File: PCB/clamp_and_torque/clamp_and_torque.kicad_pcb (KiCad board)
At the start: 2 copper layers, 4 parts, among them J3 LimitSwitches

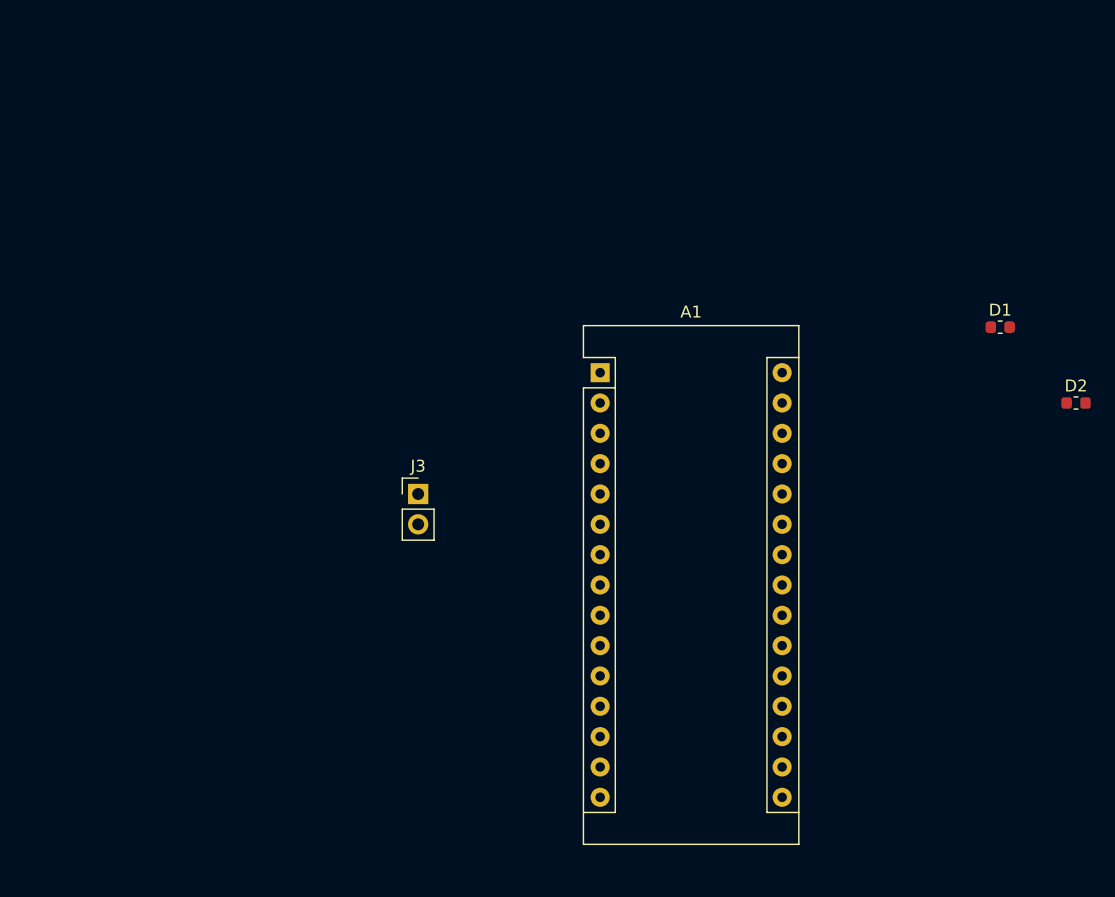
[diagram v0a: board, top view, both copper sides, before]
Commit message: Update some footprints and add a few more components.
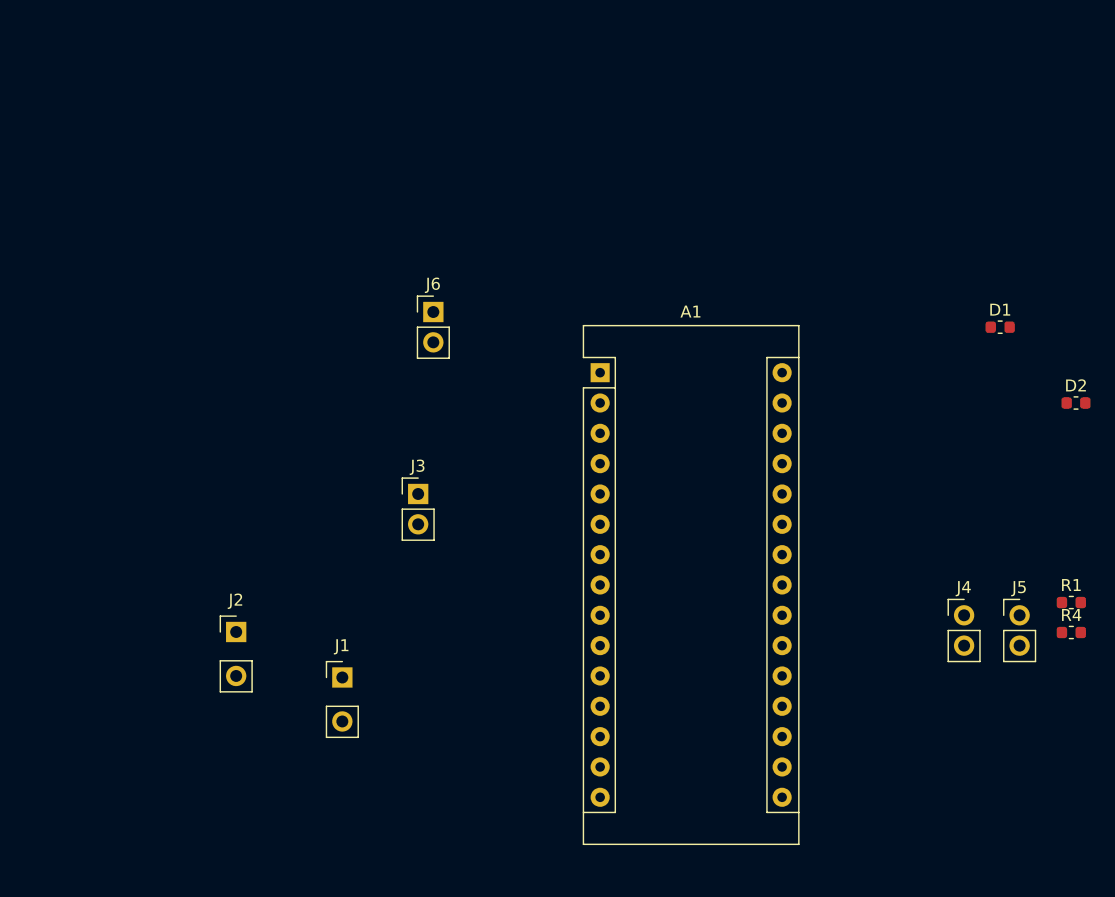
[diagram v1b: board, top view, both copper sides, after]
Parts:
- added J1: Servo1, Connector_PinHeader_2.54mm:PinHeader_1x02_P5.04mm_Vertical, F.Cu at (123.2, 125.7)
- added J2: Servo2, Connector_PinHeader_2.54mm:PinHeader_1x02_P5.04mm_Vertical, F.Cu at (114.3, 121.9)
- added J4: Conn_01x02_Female, Connector_PinHeader_2.54mm:PinHeader_1x02_P2.54mm_Vertical_V2, F.Cu at (175.3, 119.4)
- added J5: Conn_01x02_Female, Connector_PinHeader_2.54mm:PinHeader_1x02_P2.54mm_Vertical_V2, F.Cu at (179.9, 119.4)
- added J6: LimitSwitchB, Connector_PinHeader_2.54mm:PinHeader_1x02_P2.54mm_Vertical, F.Cu at (130.8, 94.0)
- added R1: 10k, Resistor_SMD:R_0603_1608Metric, F.Cu at (184.2, 118.3)
- added R4: 10k, Resistor_SMD:R_0603_1608Metric, F.Cu at (184.2, 120.8)
- J3: value LimitSwitches -> LimitSwitchA
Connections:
- A1 pad 29: Net-(A1-Pad29) -> GND
- A1 pad 5: Net-(A1-Pad5) -> D2
- A1 pad 6: Net-(A1-Pad6) -> D3
- J3 pad 1: Net-(A1-Pad6) -> GND
- J3 pad 2: Net-(A1-Pad5) -> D3

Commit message: Cleaned up schematic and roughly placed all components.
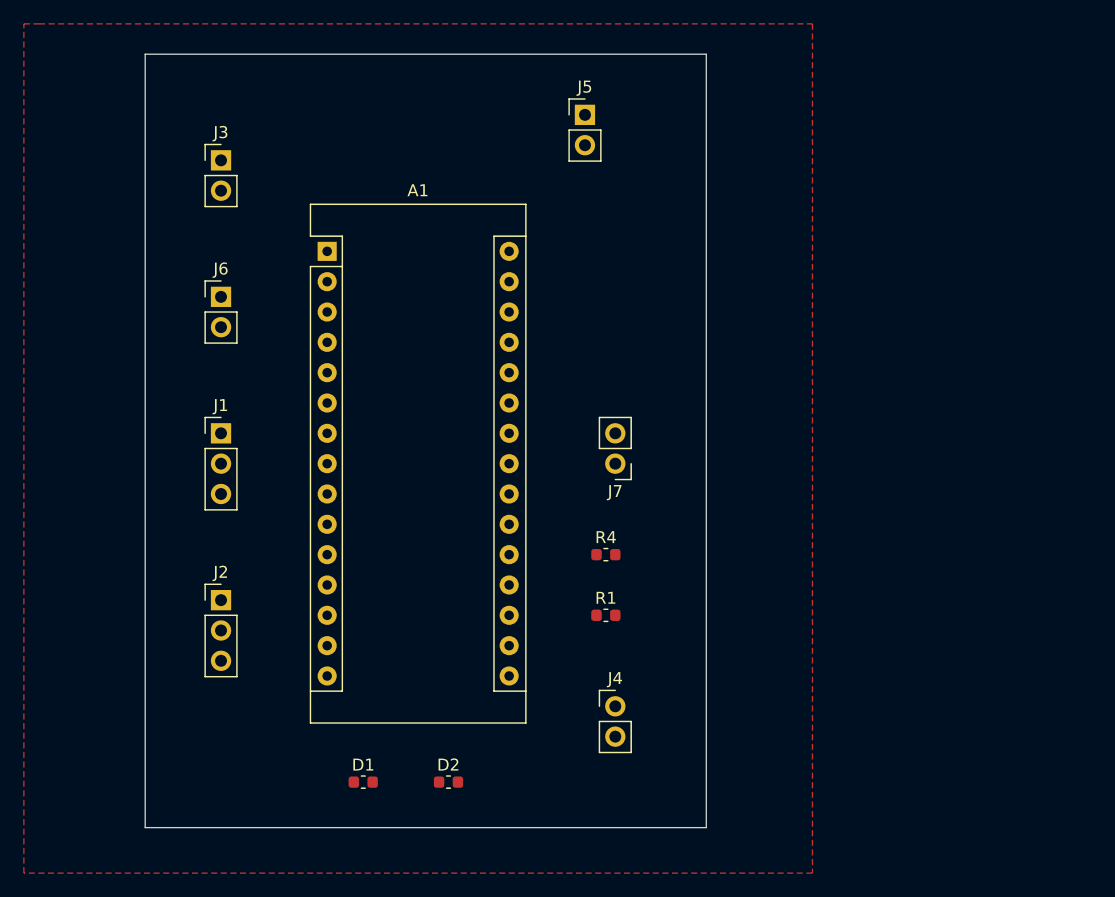
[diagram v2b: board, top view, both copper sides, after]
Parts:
- added J7: Conn_01x02_Female, Connector_PinHeader_2.54mm:PinHeader_1x02_P2.54mm_Vertical_V2, F.Cu at (146.1, 106.7)
- J1, J2: footprint Connector_PinHeader_2.54mm:PinHeader_1x02_P5.04mm_Vertical -> Connector_PinHeader_2.54mm:PinHeader_1x03_P2.54mm_Vertical
- J5: footprint Connector_PinHeader_2.54mm:PinHeader_1x02_P2.54mm_Vertical_V2 -> Connector_PinHeader_2.54mm:PinHeader_1x02_P2.54mm_Vertical
- moved D1 65.5 mm to (124.9, 133.3)
- moved D2 61.4 mm to (132.1, 133.3)
- moved J5 55.5 mm to (143.5, 77.5)
- moved R4 39.5 mm to (145.3, 114.3)
- moved R1 39.0 mm to (145.3, 119.4)
- moved J3 32.5 mm to (113.0, 81.3)
- moved J4 30.2 mm to (146.1, 127.0)
- moved A1 25.0 mm to (121.9, 88.9)
- moved J1 23.9 mm to (113.0, 104.1)
- moved J6 17.8 mm to (113.0, 92.7)
- moved J2 4.02 mm to (113.0, 118.1)
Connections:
- net Net-(A1-Pad1) renamed TX
- net Net-(A1-Pad15) renamed D12
- net Net-(A1-Pad16) renamed D13
- net Net-(A1-Pad19) renamed A0
- net Net-(A1-Pad2) renamed RX
- A1 pad 11: Net-(A1-Pad11) -> D8
- A1 pad 12: Net-(A1-Pad12) -> D9
- A1 pad 20: Net-(A1-Pad20) -> A1
- A1 pad 27: +5V -> Net-(A1-Pad27)
- A1 pad 30: Net-(A1-Pad30) -> +5V
- J1 pad 1: Net-(A1-Pad12) -> D8
- J1 pad 2: +5P -> +5V
- J2 pad 1: Net-(A1-Pad9) -> D9
- J2 pad 2: +5P -> +5V
- J3 pad 2: D3 -> D2
- J5 pad 2: Net-(A1-Pad21) -> GND
- J6 pad 2: D2 -> D3
- R4 pad 2: Net-(A1-Pad21) -> A1
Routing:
- added copper zone on F.Cu, net GND
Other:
- board outline added: 47 x 64.8 mm
